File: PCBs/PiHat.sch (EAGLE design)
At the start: 19 parts, among them IC1 TPS77030

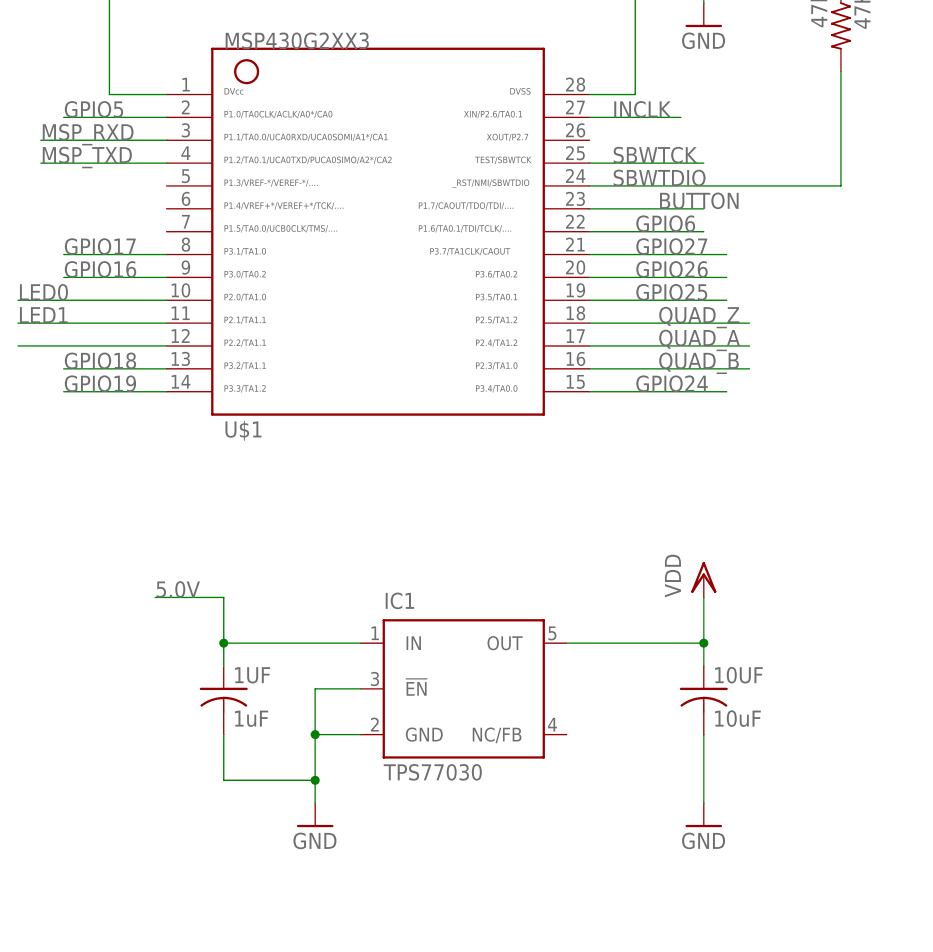
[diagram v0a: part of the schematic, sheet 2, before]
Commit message: Updated board after debugging first revision
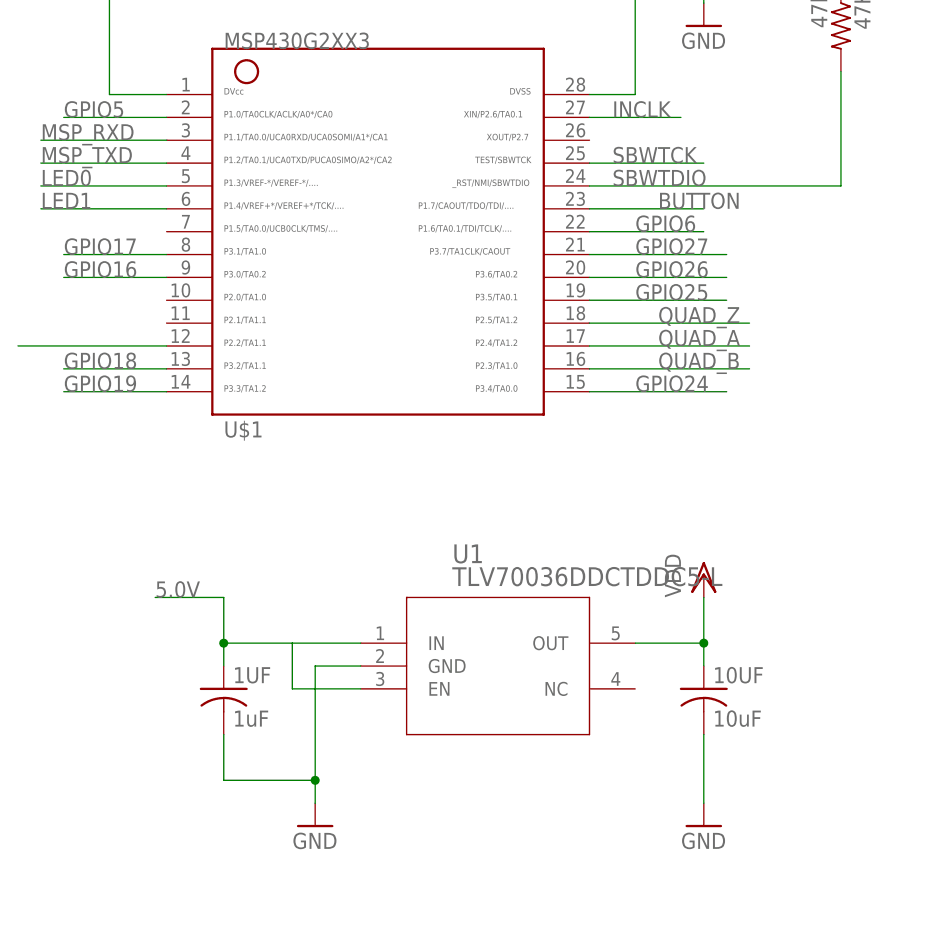
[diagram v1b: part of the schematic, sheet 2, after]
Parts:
- removed IC1: TPS77030, texas:TPS77030
- added U1: TLV70036DDCTDDC5-L, TLV70036:TLV70036DDCTDDC5-L
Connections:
- net 5.0V: now also U1.EN, U1.IN; no longer IC1.IN
- net GND: now also U1.GND; no longer IC1.!EN, IC1.GND
- net LED0: now also U$1.5; no longer U$1.10
- net LED1: now also U$1.6; no longer U$1.11
- net VDD: now also U1.OUT; no longer IC1.OUT
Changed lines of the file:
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@@
 <part name="VDD1" library="supply1" library_urn="urn:adsk.eagle:library:371" deviceset="VDD" device=""/>
 <part name="GND8" library="supply1" library_urn="urn:adsk.eagle:library:371" deviceset="GND" device=""/>
-<part name="IC1" library="texas" library_urn="urn:adsk.eagle:library:387" deviceset="TPS770*" device="" technology="30"/>
 <part name="10UF" library="rcl" library_urn="urn:adsk.eagle:library:334" deviceset="C-US" device="C1206" package3d_urn="urn:adsk.eagle:package:23618/2" value="10uF"/>
 <part name="1UF" library="rcl" library_urn="urn:adsk.eagle:library:334" deviceset="C-US" device="C0603" package3d_urn="urn:adsk.eagle:package:23616/2" value="1uF"/>
@@
 <part name="PROGRAM" library="con-lstb-mod" deviceset="MA07-1" device="" package3d_urn="urn:adsk.eagle:package:8341/1"/>
 <part name="AMT102" library="con-lstb-mod" deviceset="MA06-1" device="" package3d_urn="urn:adsk.eagle:package:8340/1"/>
+<part name="U1" library="TLV70036" deviceset="TLV70036DDCT" device="DDC5-L"/>
 </parts>
 <sheets>
@@
 <attribute name="VALUE" x="-73.66" y="-45.72" size="1.778" layer="96"/>
 </instance>
-<instance part="IC1" gate="G$1" x="-55.88" y="-27.94" smashed="yes">
-<attribute name="NAME" x="-63.5" y="-19.05" size="1.778" layer="95"/>
-<attribute name="VALUE" x="-63.5" y="-38.1" size="1.778" layer="96"/>
-</instance>
 <instance part="10UF" gate="G$1" x="-27.94" y="-27.94" smashed="yes">
 <attribute name="NAME" x="-26.924" y="-27.305" size="1.778" layer="95"/>
@@
 <attribute name="VALUE" x="87.63" y="38.1" size="1.778" layer="96"/>
 <attribute name="NAME" x="87.63" y="59.182" size="1.778" layer="95"/>
+</instance>
+<instance part="U1" gate="A" x="-68.58" y="-22.86" smashed="yes">
+<attribute name="NAME" x="-55.88" y="-13.97" size="2.0828" layer="95" ratio="6" rot="SR0"/>
+<attribute name="VALUE" x="-55.88" y="-16.51" size="2.0828" layer="96" ratio="6" rot="SR0"/>
 </instance>
 </instances>
@@
 </segment>
 <segment>
-<pinref part="IC1" gate="G$1" pin="OUT"/>
-<wire x1="-43.18" y1="-22.86" x2="-27.94" y2="-22.86" width="0.1524" layer="91"/>
+<wire x1="-35.56" y1="-22.86" x2="-27.94" y2="-22.86" width="0.1524" layer="91"/>
 <wire x1="-27.94" y1="-22.86" x2="-27.94" y2="-17.78" width="0.1524" layer="91"/>
 <pinref part="VDD5" gate="G$1" pin="VDD"/>
@@
 <wire x1="-27.94" y1="-22.86" x2="-27.94" y2="-25.4" width="0.1524" layer="91"/>
 <pinref part="10UF" gate="G$1" pin="1"/>
+<pinref part="U1" gate="A" pin="OUT"/>
 </segment>
 <segment>
@@
 </segment>
 <segment>
-<pinref part="IC1" gate="G$1" pin="GND"/>
-<wire x1="-66.04" y1="-33.02" x2="-71.12" y2="-33.02" width="0.1524" layer="91"/>
 <pinref part="GND8" gate="1" pin="GND"/>
-<wire x1="-71.12" y1="-33.02" x2="-71.12" y2="-38.1" width="0.1524" layer="91"/>
-<pinref part="IC1" gate="G$1" pin="!EN"/>
 <wire x1="-71.12" y1="-38.1" x2="-71.12" y2="-40.64" width="0.1524" layer="91"/>
-<wire x1="-66.04" y1="-27.94" x2="-71.12" y2="-27.94" width="0.1524" layer="91"/>
-<wire x1="-71.12" y1="-27.94" x2="-71.12" y2="-33.02" width="0.1524" layer="91"/>
-<junction x="-71.12" y="-33.02"/>
+<wire x1="-66.04" y1="-25.4" x2="-71.12" y2="-25.4" width="0.1524" layer="91"/>
+<wire x1="-71.12" y1="-25.4" x2="-71.12" y2="-38.1" width="0.1524" layer="91"/>
 <pinref part="1UF" gate="G$1" pin="2"/>
 <wire x1="-81.28" y1="-33.02" x2="-81.28" y2="-38.1" width="0.1524" layer="91"/>
 <wire x1="-81.28" y1="-38.1" x2="-71.12" y2="-38.1" width="0.1524" layer="91"/>
 <junction x="-71.12" y="-38.1"/>
+<pinref part="U1" gate="A" pin="GND"/>
 </segment>
 <segment>
@@
 <net name="5.0V" class="0">
 <segment>
-<pinref part="IC1" gate="G$1" pin="IN"/>
-<wire x1="-66.04" y1="-22.86" x2="-81.28" y2="-22.86" width="0.1524" layer="91"/>
+<wire x1="-66.04" y1="-22.86" x2="-73.66" y2="-22.86" width="0.1524" layer="91"/>
+<wire x1="-73.66" y1="-22.86" x2="-81.28" y2="-22.86" width="0.1524" layer="91"/>
 <wire x1="-81.28" y1="-22.86" x2="-81.28" y2="-17.78" width="0.1524" layer="91"/>
 <wire x1="-81.28" y1="-17.78" x2="-88.9" y2="-17.78" width="0.1524" layer="91"/>
@@
 <wire x1="-81.28" y1="-22.86" x2="-81.28" y2="-25.4" width="0.1524" layer="91"/>
 <junction x="-81.28" y="-22.86"/>
+<pinref part="U1" gate="A" pin="IN"/>
+<wire x1="-73.66" y1="-22.86" x2="-73.66" y2="-27.94" width="0.1524" layer="91"/>
+<pinref part="U1" gate="A" pin="EN"/>
+<wire x1="-73.66" y1="-27.94" x2="-66.04" y2="-27.94" width="0.1524" layer="91"/>
 </segment>
 </net>
@@
 </segment>
 <segment>
-<pinref part="U$1" gate="G$1" pin="11"/>
-<wire x1="-87.63" y1="12.7" x2="-104.14" y2="12.7" width="0.1524" layer="91"/>
-<label x="-104.14" y="12.7" size="1.778" layer="95"/>
+<pinref part="U$1" gate="G$1" pin="6"/>
+<wire x1="-87.63" y1="25.4" x2="-101.6" y2="25.4" width="0.1524" layer="91"/>
+<label x="-101.6" y="25.4" size="1.778" layer="95"/>
 </segment>
 </net>
@@
 </segment>
 <segment>
-<pinref part="U$1" gate="G$1" pin="10"/>
-<wire x1="-87.63" y1="15.24" x2="-104.14" y2="15.24" width="0.1524" layer="91"/>
-<label x="-104.14" y="15.24" size="1.778" layer="95"/>
-</segment>
-</net>
+<pinref part="U$1" gate="G$1" pin="5"/>
+<wire x1="-87.63" y1="27.94" x2="-101.6" y2="27.94" width="0.1524" layer="91"/>
+<label x="-101.6" y="27.94" size="1.778" layer="95"/>
+</segment>
+</net>
